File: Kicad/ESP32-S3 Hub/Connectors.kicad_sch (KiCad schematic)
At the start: 23 parts, among them J1 1.27mm 3pin socket, J10 1.27mm 3pin socket, J11 7 pin FPC 0.3mm Panasonic Y3b, J12 1.27mm 3pin socket, J13 TE 3-2363961-0 receptacle, J14 TE 3-2363962-0 Connector, J16 TE 3-2363961-0 receptacle, J17 TE 3-2363962-0 Connector, J2 1.27mm 3pin socket, J21 1.27mm 4 pin socket, J22 1.27mm 4 pin header, J3 7 pin FPC 0.3mm Panasonic Y3b, J4 1.27mm 3pin socket, J5 7 pin FPC 0.3mm Panasonic Y3b, J6 1.27mm 3pin socket, J7 1.27mm 3pin socket, J8 7 pin FPC 0.3mm Panasonic Y3b, J9 1.27mm 3pin socket

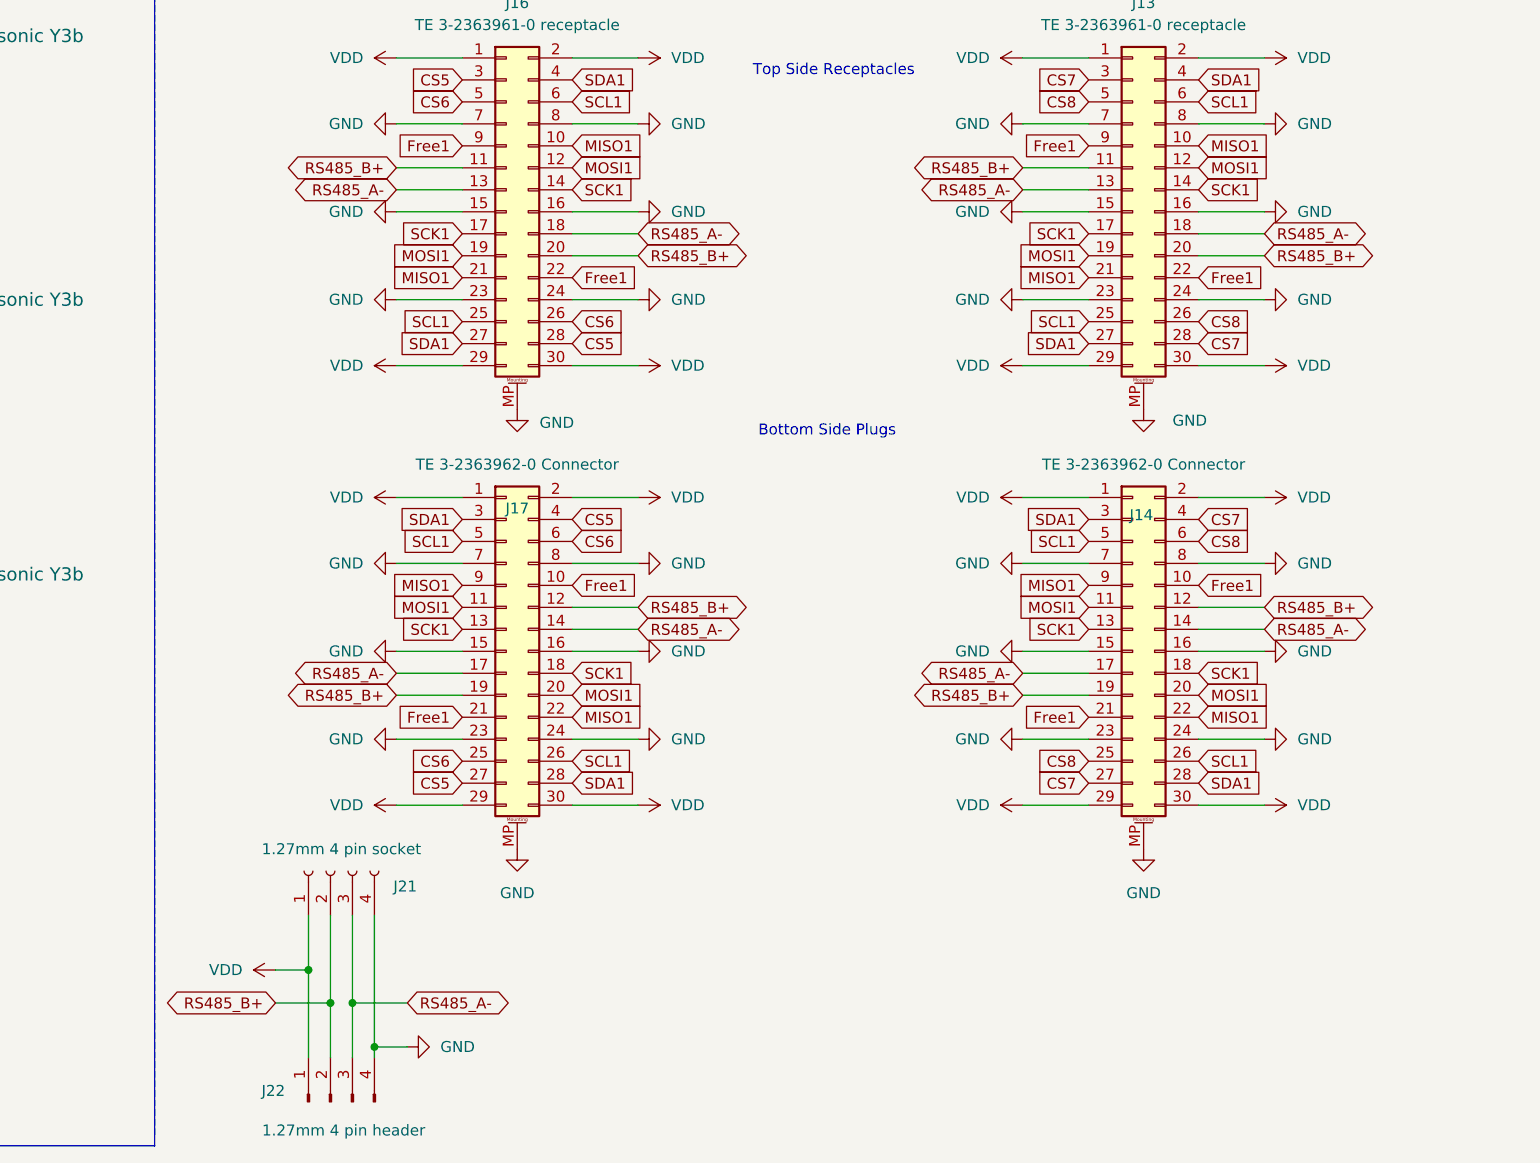
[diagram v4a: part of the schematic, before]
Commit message: Swapping register pins
I tryid to simplify the layout a little bit. I also added a note about the potential danger of the i2c lines on low level glitching pins.
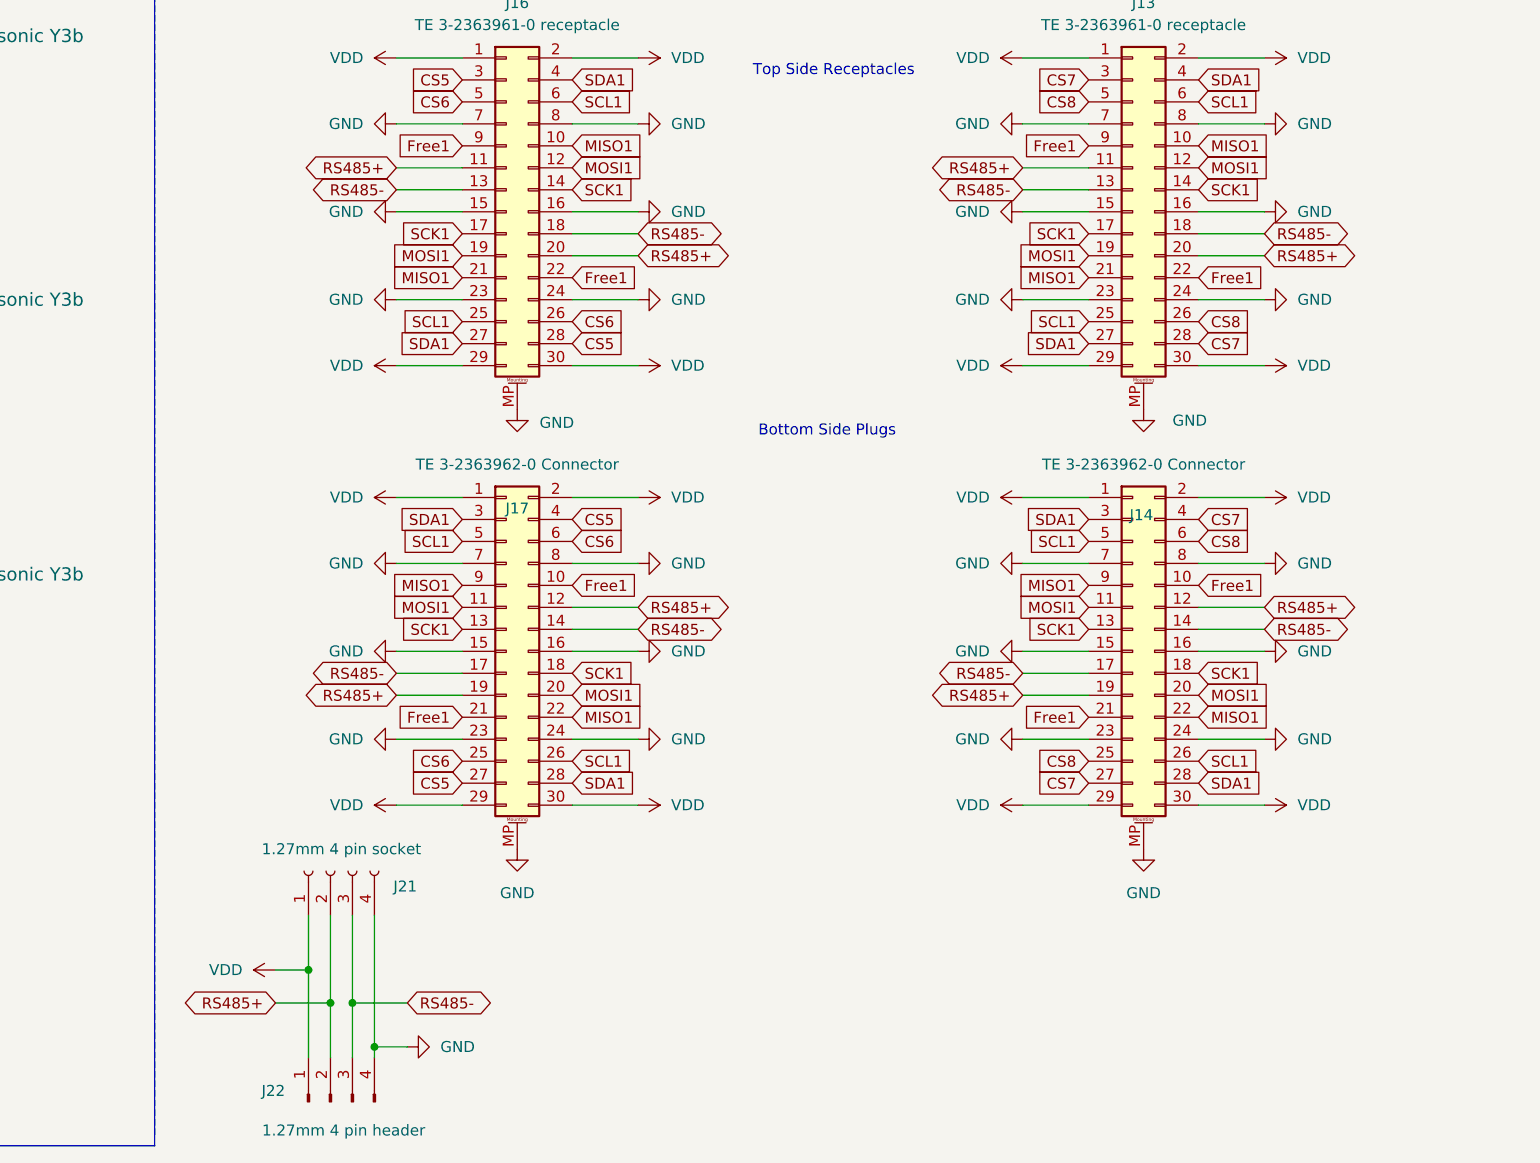
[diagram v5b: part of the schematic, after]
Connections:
- net RS485_A- renamed RS485-
- net RS485_B+ renamed RS485+

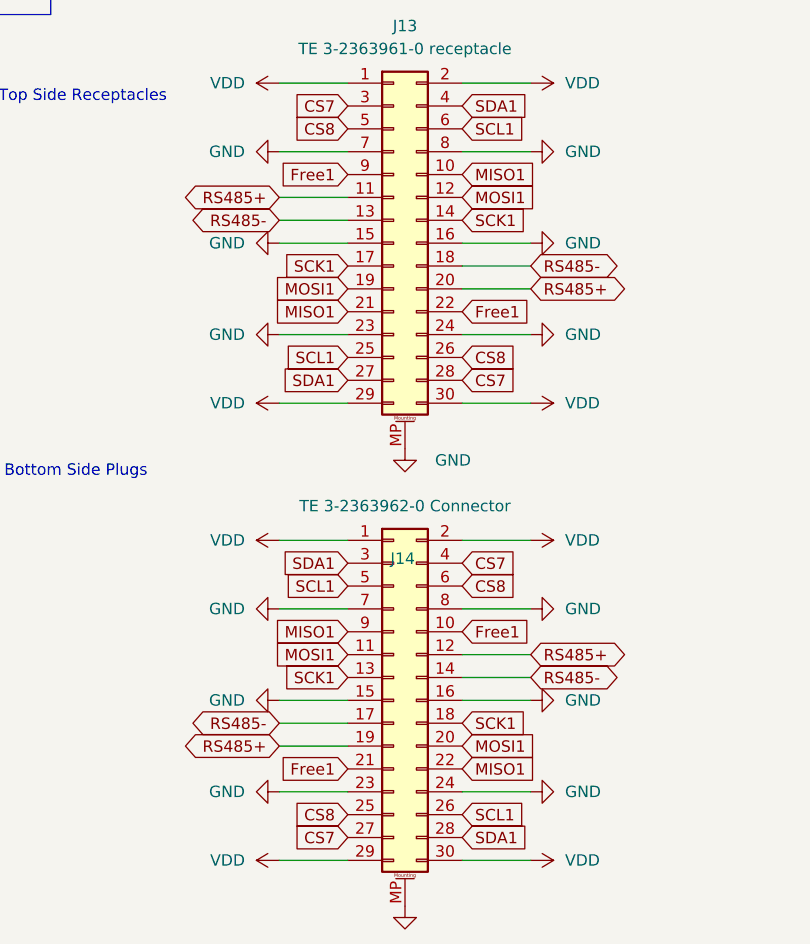
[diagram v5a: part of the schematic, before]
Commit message: Changed layer stack
I now have a layer stack of Sig/Gnd/Sig/Pwr/Gnd/Sig, which appears to be a common arrangement except I've reversed the order. I added a lot of signals in the middle of the power layer though, because I need more space and I previously had too many signals on my dedicated ground plane.

I also connected Free2 to the correct connectors in the schematic, something I missed when I changed the esp32 pin assignments.
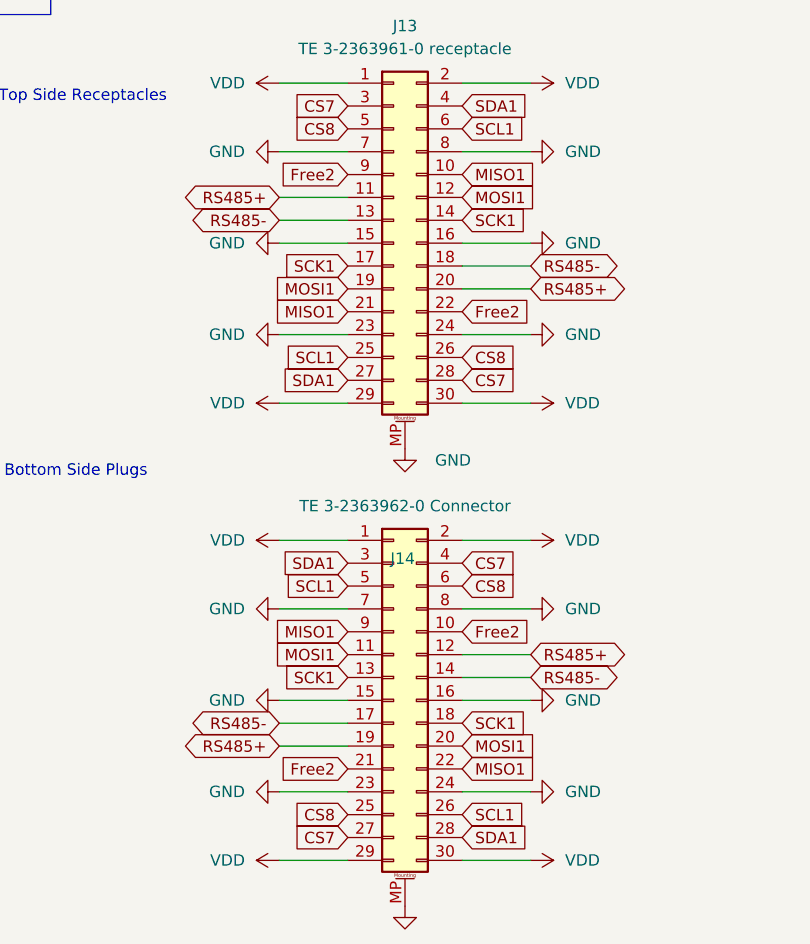
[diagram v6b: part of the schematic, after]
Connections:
- net Free1: no longer J13.22 (Pin_22), J13.9 (Pin_9), J14.10 (Pin_10), J14.21 (Pin_21)
- new net Free2: J13.22 (Pin_22), J13.9 (Pin_9), J14.10 (Pin_10), J14.21 (Pin_21)
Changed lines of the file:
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@@
-		)
-	)
-	(global_label "Free1"
-		(shape input)
-		(at 241.3 149.86 180)
-		(fields_autoplaced yes)
-		(effects
-			(font
-				(size 1.27 1.27)
-			)
-			(justify right)
-		)
-		(property "Intersheetrefs" "${INTERSHEET_REFS}"
-			(at 233.0533 149.86 0)
-			(effects
-				(font
-					(size 1.27 1.27)
-				)
-				(justify right)
-				(hide yes)
-			)
 		)
 	)
@@
 		(property "Intersheetrefs" "${INTERSHEET_REFS}"
 			(at 261.7628 76.2 0)
-			(effects
-				(font
-					(size 1.27 1.27)
-				)
-				(justify left)
-				(hide yes)
-			)
-		)
-	)
-	(global_label "Free1"
-		(shape input)
-		(at 254 134.62 0)
-		(fields_autoplaced yes)
-		(effects
-			(font
-				(size 1.27 1.27)
-			)
-			(justify left)
-		)
-		(property "Intersheetrefs" "${INTERSHEET_REFS}"
-			(at 262.2467 134.62 0)
 			(effects
 				(font
@@
 		)
 	)
-	(global_label "Free1"
-		(shape input)
-		(at 241.3 83.82 180)
-		(fields_autoplaced yes)
-		(effects
-			(font
-				(size 1.27 1.27)
-			)
-			(justify right)
-		)
-		(property "Intersheetrefs" "${INTERSHEET_REFS}"
-			(at 233.0533 83.82 0)
-			(effects
-				(font
-					(size 1.27 1.27)
-				)
-				(justify right)
-				(hide yes)
-			)
-		)
-	)
 	(global_label "MOSI1"
 		(shape input)
@@
 		)
 	)
+	(global_label "Free2"
+		(shape input)
+		(at 241.3 83.82 180)
+		(fields_autoplaced yes)
+		(effects
+			(font
+				(size 1.27 1.27)
+			)
+			(justify right)
+		)
+		(property "Intersheetrefs" "${INTERSHEET_REFS}"
+			(at 233.0533 83.82 0)
+			(effects
+				(font
+					(size 1.27 1.27)
+				)
+				(justify right)
+				(hide yes)
+			)
+		)
+	)
 	(global_label "RS485-"
 		(shape bidirectional)
@@
 		)
 	)
+	(global_label "Free2"
+		(shape input)
+		(at 241.3 149.86 180)
+		(fields_autoplaced yes)
+		(effects
+			(font
+				(size 1.27 1.27)
+			)
+			(justify right)
+		)
+		(property "Intersheetrefs" "${INTERSHEET_REFS}"
+			(at 233.0533 149.86 0)
+			(effects
+				(font
+					(size 1.27 1.27)
+				)
+				(justify right)
+				(hide yes)
+			)
+		)
+	)
 	(global_label "MISO1"
 		(shape input)
@@
 		)
 	)
+	(global_label "Free2"
+		(shape input)
+		(at 254 134.62 0)
+		(fields_autoplaced yes)
+		(effects
+			(font
+				(size 1.27 1.27)
+			)
+			(justify left)
+		)
+		(property "Intersheetrefs" "${INTERSHEET_REFS}"
+			(at 262.2467 134.62 0)
+			(effects
+				(font
+					(size 1.27 1.27)
+				)
+				(justify left)
+				(hide yes)
+			)
+		)
+	)
 	(global_label "SDA1"
 		(shape input)
@@
 		)
 	)
-	(global_label "Free1"
-		(shape input)
-		(at 254 99.06 0)
-		(fields_autoplaced yes)
-		(effects
-			(font
-				(size 1.27 1.27)
-			)
-			(justify left)
-		)
-		(property "Intersheetrefs" "${INTERSHEET_REFS}"
-			(at 262.2467 99.06 0)
-			(effects
-				(font
-					(size 1.27 1.27)
-				)
-				(justify left)
-				(hide yes)
-			)
-		)
-	)
 	(global_label "SCL1"
 		(shape input)
@@
 			(effects
 				(font
+					(size 1.27 1.27)
+				)
+				(justify left)
+				(hide yes)
+			)
+		)
+	)
+	(global_label "Free2"
+		(shape input)
+		(at 254 99.06 0)
+		(fields_autoplaced yes)
+		(effects
+			(font
+				(size 1.27 1.27)
+			)
+			(justify left)
+		)
+		(property "Intersheetrefs" "${INTERSHEET_REFS}"
+			(at 262.2467 99.06 0)
+			(effects
+				(font
